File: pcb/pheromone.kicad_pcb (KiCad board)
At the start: 2 copper layers, 304 x 99 mm, 158 parts, among them J1 USB_B_Micro, K1 KEYSW, K10 KEYSW, K11 KEYSW, K12 KEYSW, K13 KEYSW, K14 KEYSW, K15 KEYSW, K16 KEYSW, K17 KEYSW, K18 KEYSW, K19 KEYSW, K2 KEYSW, K20 KEYSW, K21 KEYSW, K22 KEYSW, K23 KEYSW, K24 KEYSW, K25 KEYSW, K26 KEYSW, K27 KEYSW, K28 KEYSW, K29 KEYSW, K3 KEYSW, K30 KEYSW, K31 KEYSW, K32 KEYSW, K33 KEYSW, K34 KEYSW, K35 KEYSW, K36 KEYSW, K37 KEYSW, K38 KEYSW, K39 KEYSW, K4 KEYSW, K40 KEYSW, K41 KEYSW, K42 KEYSW, K43 KEYSW, K44 KEYSW, K45 KEYSW, K46 KEYSW, K47 KEYSW, K48 KEYSW, K49 KEYSW, K5 KEYSW, K50 KEYSW, K51 KEYSW, K52 KEYSW, K53 KEYSW, K54 KEYSW, K55 KEYSW, K56 KEYSW, K57 KEYSW, K58 KEYSW, K59 KEYSW, K6 KEYSW, K60 KEYSW, K61 KEYSW, K62 KEYSW, K63 KEYSW, K7 KEYSW, K8 KEYSW, K9 KEYSW, P1 AVR-ISP-6, SW1 SW_PUSH, U1 ATMEGA32U4, Y1 Crystal_GND24

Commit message: add typec support
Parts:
- removed G***: LOGO, LOGO:monitor
- removed G***: LOGO, LOGO:warning
- removed G***: LOGO, LOGO:brand
- removed G***: LOGO, LOGO:bulb
- removed REF**: KiCad-Logo_5mm_Copper, Symbol:KiCad-Logo_5mm_Copper
- removed REF**: WEEE-Logo_4.2x6mm_SilkScreen, Symbol:WEEE-Logo_4.2x6mm_SilkScreen
- removed [SCREW] (x6): MountingHole_2.2mm_M2, MountingHole:MountingHole_2.2mm_M2
- added D64: 3.6V, Diode_SMD:D_SOD-123, F.Cu at (47.0, 53.3)
- added D65: 3.6v, Diode_SMD:D_SOD-123, F.Cu at (43.2, 57.1)
- added F1: 500mA, Fuse:Fuse_0805_2012Metric, F.Cu at (50.8, 62.2)
- added R5: 5.1k, Resistor_SMD:R_0805_2012Metric, F.Cu at (45.7, 68.6)
- added R6: 75, Resistor_SMD:R_0805_2012Metric, B.Cu at (49.5, 68.6)
- added R7: 75, Resistor_SMD:R_0805_2012Metric, B.Cu at (47.0, 64.8)
- J1: value USB_B_Micro -> USB_C_Receptacle; footprint Connector_USB:USB_Micro-B_Molex-105017-0001 -> Connector_USB:USB_C_Receptacle_GCT_USB4085; moved to F.Cu
- R1: value 22 -> 1.5k; moved to F.Cu
- R2: value 22 -> 5.1k
- moved R1 8.71 mm to (50.8, 58.4), turned to 0 degrees
- moved J1 5.24 mm to (43.2, 62.2), turned to 270 degrees
- moved R2 3.42 mm to (47.0, 61.0), turned to 270 degrees
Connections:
- E1 pad S1: Net-(E1-PadS1) -> (no net)
- E1 pad S2: Net-(E1-PadS2) -> (no net)
- R1 pad 1: Net-(R1-Pad1) -> Net-(D64-Pad1)
- R1 pad 2: Net-(J1-Pad2) -> VCC
- R2 pad 1: Net-(R2-Pad1) -> GND
- R2 pad 2: Net-(J1-Pad3) -> Net-(J1-PadA5)
- U1 pad 3: Net-(R1-Pad1) -> D-
- U1 pad 4: Net-(R2-Pad1) -> D+
- U1 pad 42: Net-(U1-Pad42) -> (no net)
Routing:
- net D+: track 0.00 -> 213.6 mm
- net Net-(R2-Pad1): track 212.8 -> 0.00 mm
- net Net-(R1-Pad1): track 211.3 -> 0.00 mm
- net D-: track 0.00 -> 210.1 mm
- net Net-(D64-Pad1): track 0.00 -> 25.0 mm, vias 0 -> 1
- net Net-(J1-PadB5): track 0.00 -> 24.1 mm
- net Net-(F1-Pad1): track 0.00 -> 17.7 mm, vias 0 -> 1
- net Net-(D65-Pad1): track 0.00 -> 14.5 mm, vias 0 -> 1
- net VCC: track 416.2 -> 407.6 mm, vias 2 -> 4
- net Net-(J1-Pad3): track 8.15 -> 0.00 mm
- net Net-(J1-Pad2): track 8.01 -> 0.00 mm
- net GND: track 68.9 -> 75.6 mm, vias 7 -> 22
- net Net-(J1-PadA5): track 0.00 -> 4.65 mm, vias 0 -> 1
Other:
- rule trace_min: 0.2 -> 0.1
- rule via_min_size: 0.4 -> 0.1

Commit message: updates pcb
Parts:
- D64, D65, R5: moved to B.Cu
- moved D64 7.41 mm to (43.2, 59.7), turned to 0 degrees
- moved R2 4.12 mm to (47.7, 65.0), turned to 180 degrees
- moved R5 3.25 mm to (47.8, 71.1), turned to 180 degrees
- moved R7 2.39 mm to (47.7, 67.1)
- moved J1 1.98 mm to (44.7, 63.5)
- moved R6 1.85 mm to (47.8, 69.1), turned to 180 degrees
- moved R1 1.37 mm to (50.3, 59.7)
- moved D65 0.76 mm to (43.2, 56.4)
- moved F1 0.51 mm to (50.3, 62.2)
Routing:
- net Net-(J1-PadB5): track 24.1 -> 10.2 mm
- net VCC: track 407.6 -> 401.5 mm
- net D+: track 213.6 -> 209.4 mm
- net Net-(D65-Pad1): track 14.5 -> 18.2 mm, vias 1 -> 0
- net Net-(F1-Pad1): track 17.7 -> 14.2 mm, vias 1 -> 0
- net Net-(D64-Pad1): track 25.0 -> 21.9 mm
- net Net-(J1-PadA5): track 4.65 -> 2.10 mm, vias 1 -> 0
- net D-: track 210.1 -> 208.8 mm
- net GND: vias 22 -> 7

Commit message: updates pcb
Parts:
- D64, D65, R2, R5, R6, R7: moved to F.Cu
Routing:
- net Net-(D64-Pad1): track 21.9 -> 25.9 mm, vias 1 -> 0
- net D+: track 209.4 -> 211.0 mm, vias 0 -> 1
- net D-: track 208.8 -> 209.5 mm, vias 0 -> 1
- net Net-(D65-Pad1): track 18.2 -> 18.8 mm
- net Net-(J1-PadB5): track 10.2 -> 9.62 mm
- net GND: vias 7 -> 10

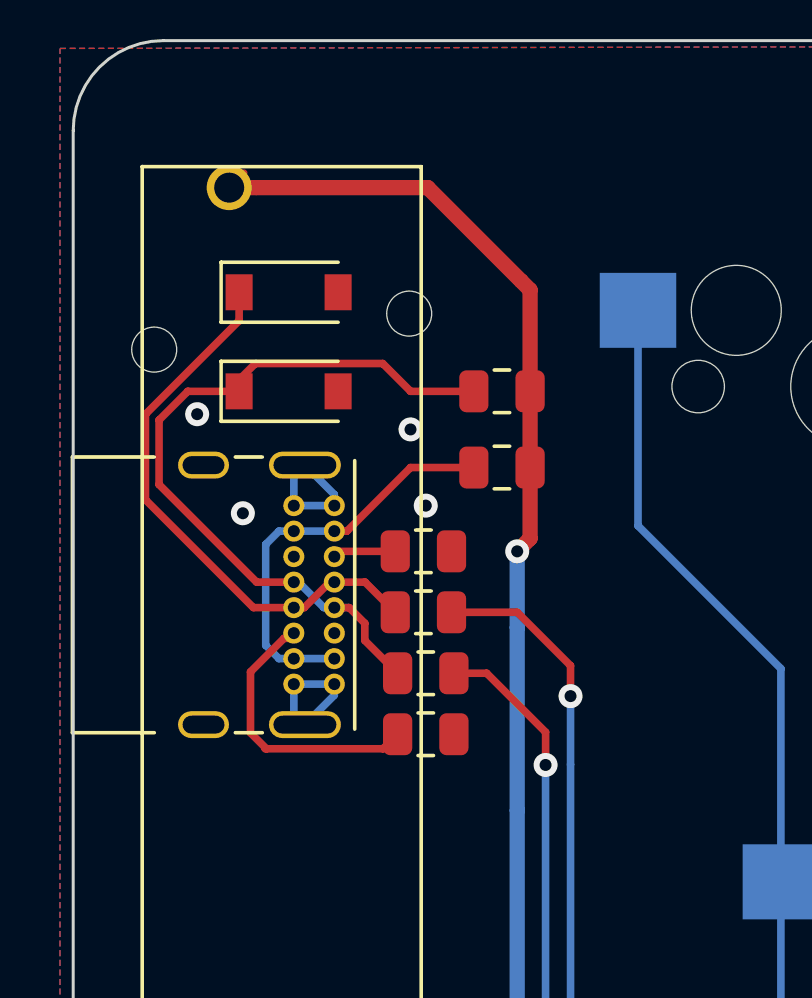
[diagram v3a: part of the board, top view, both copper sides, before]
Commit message: flip side for typec connector
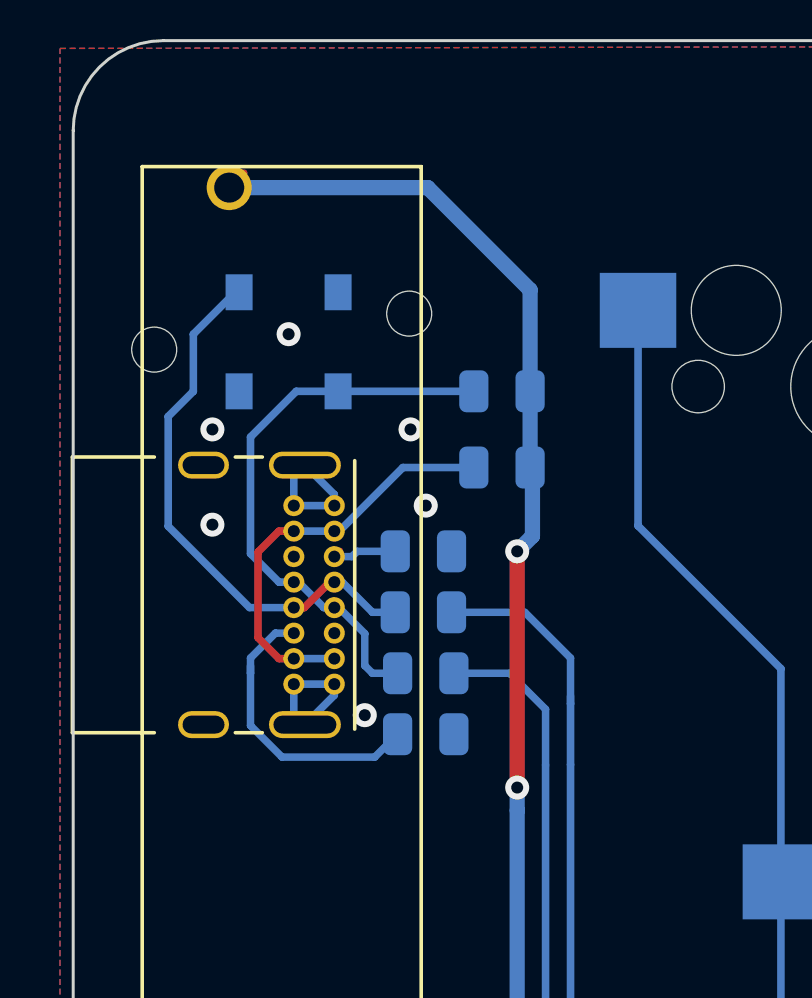
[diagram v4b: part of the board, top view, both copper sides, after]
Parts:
- D64, D65, F1, R1, R2, R5, R6, R7: moved to B.Cu
- turned D64 to 180 degrees
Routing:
- net Net-(D64-Pad1): track 25.9 -> 19.3 mm
- net Net-(J1-PadB5): track 9.62 -> 10.3 mm
- net D-: track 209.5 -> 209.9 mm, vias 1 -> 0
- net D+: track 211.0 -> 211.4 mm, vias 1 -> 0
- net VCC: vias 4 -> 5
- net GND: vias 10 -> 12

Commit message: update silks and other stuff
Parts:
- moved R2 0.08 mm to (47.8, 65.0)
- moved R7 0.08 mm to (47.8, 67.1)
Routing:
- net GND: vias 12 -> 10
